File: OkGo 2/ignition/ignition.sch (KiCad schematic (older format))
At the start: 26 parts

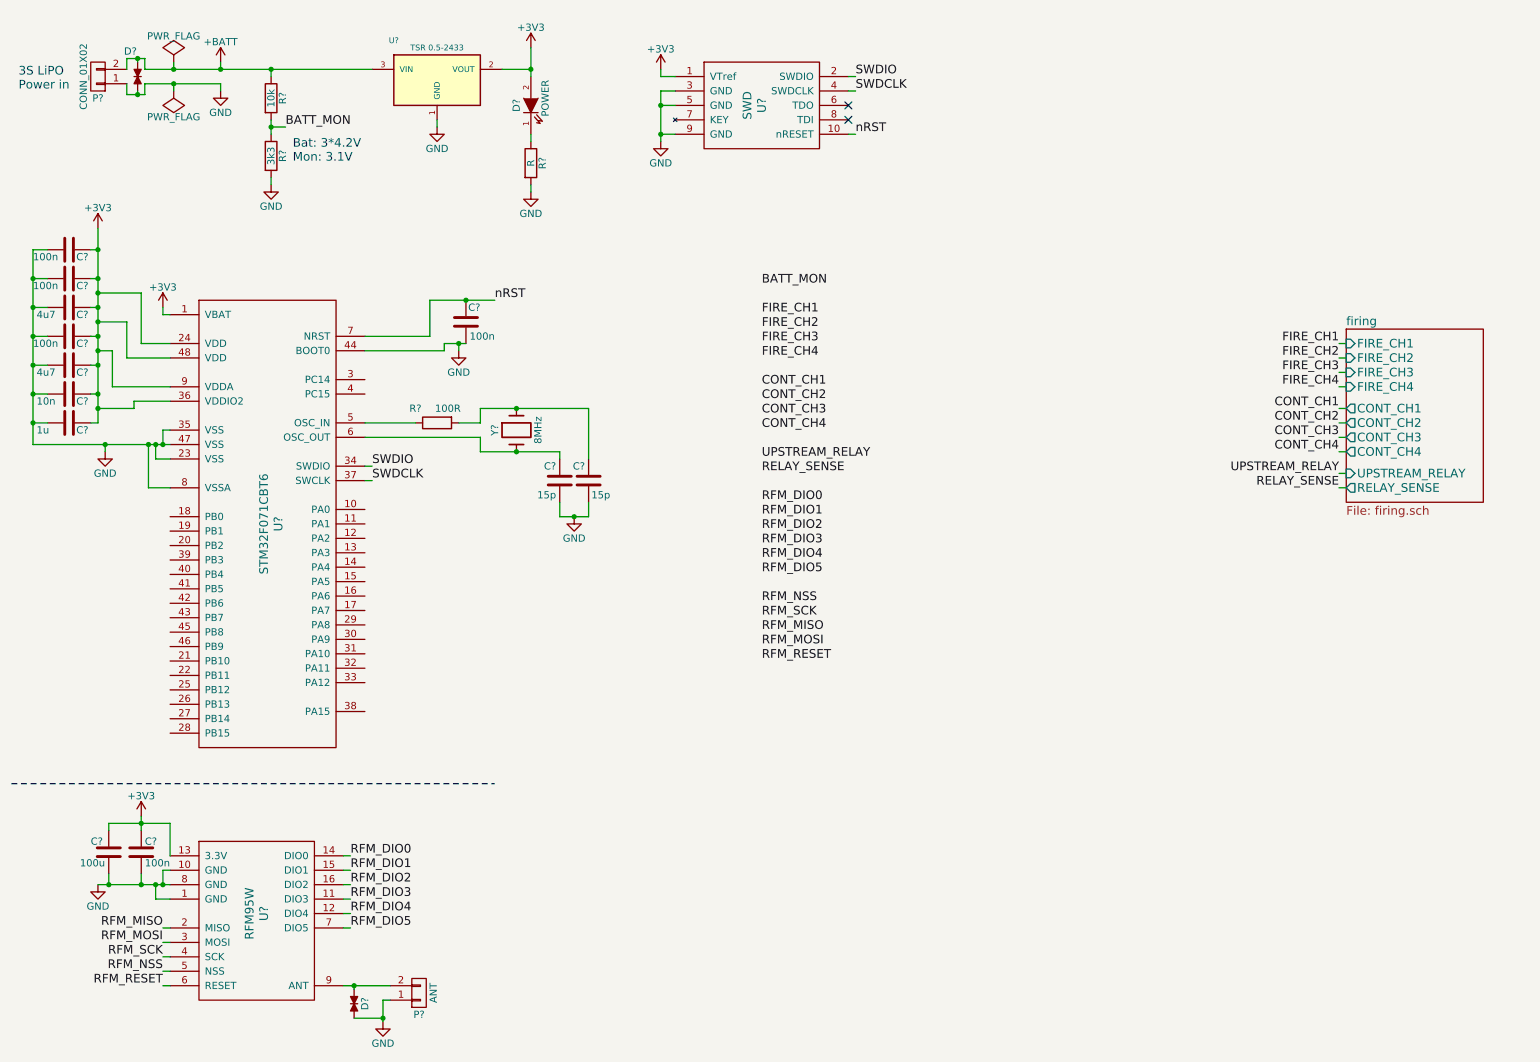
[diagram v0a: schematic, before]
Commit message: Removed pin labels from TVS
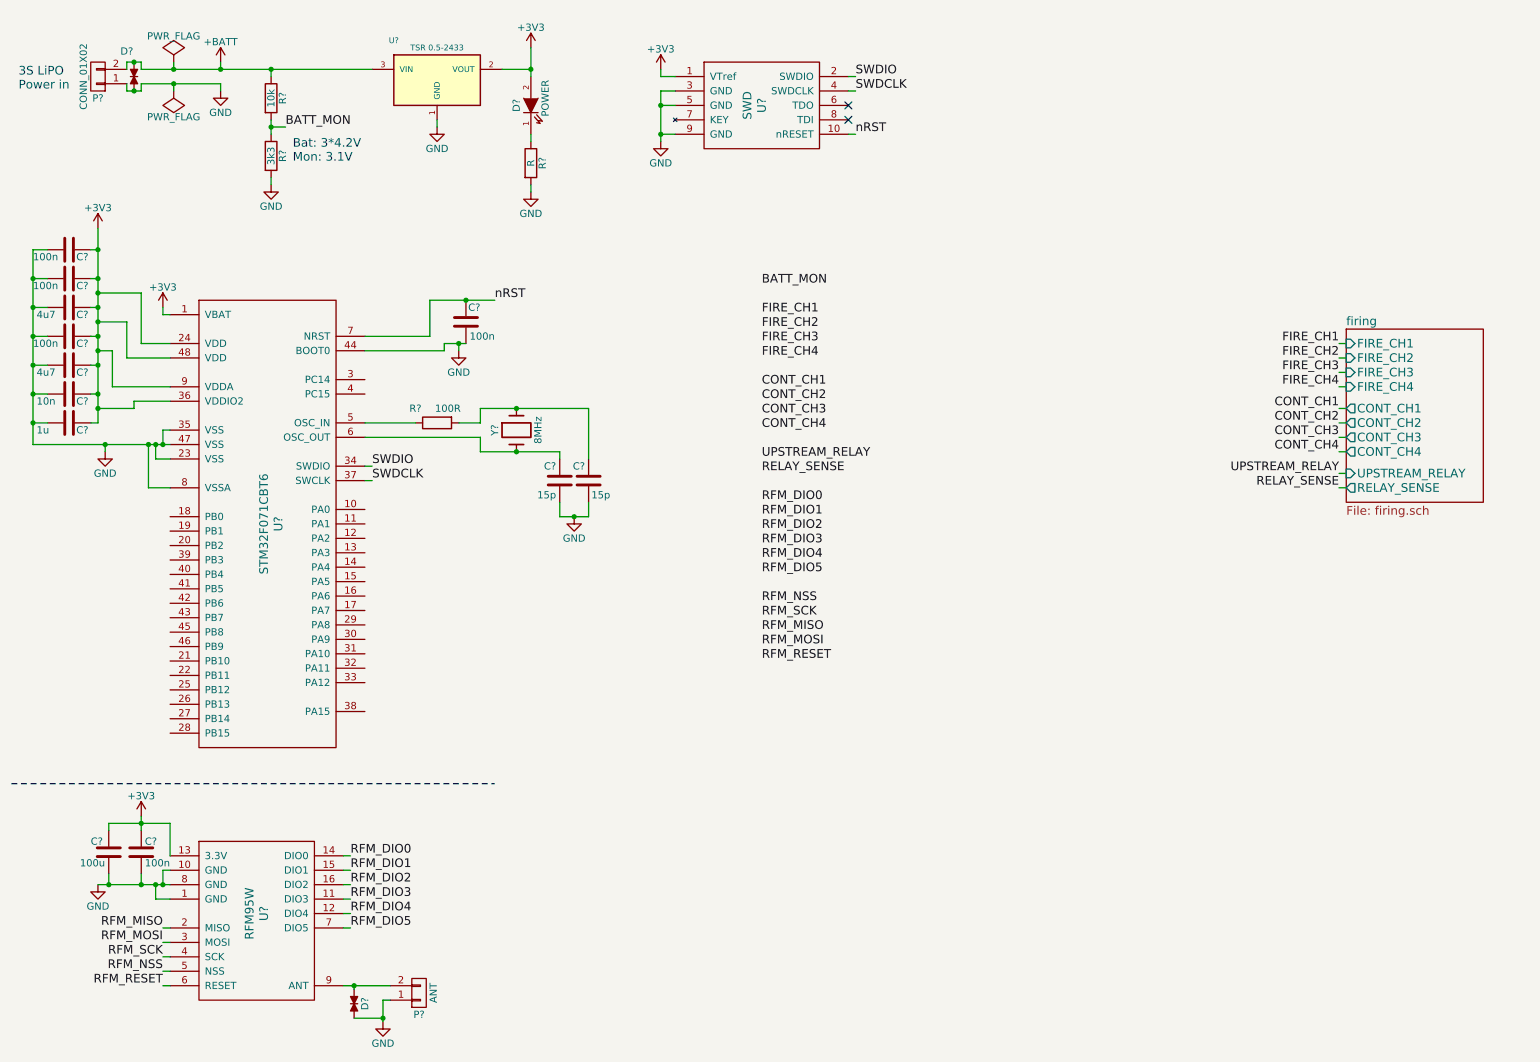
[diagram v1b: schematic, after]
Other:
- moved on the sheet: D?
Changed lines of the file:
@@
 L TVS_small D?
 U 1 1 559D6477
-P 1375 1000
-F 0 "D?" V 1200 950 50  0000 C CNN
-F 1 "TVS_small" H 1375 925 50  0001 C CNN
-F 2 "Resistors_SMD:R_0603_HandSoldering" H 1375 1000 60  0001 C CNN
-F 3 "" H 1375 1000 60  0000 C CNN
-F 4 "2368174" H 1375 1000 60  0001 C CNN "Farnell"
-	1    1375 1000
+P 1350 1000
+F 0 "D?" V 1175 950 50  0000 C CNN
+F 1 "TVS_small" H 1350 925 50  0001 C CNN
+F 2 "Resistors_SMD:R_0603_HandSoldering" H 1350 1000 60  0001 C CNN
+F 3 "" H 1350 1000 60  0000 C CNN
+F 4 "2368174" H 1350 1000 60  0001 C CNN "Farnell"
+	1    1350 1000
 	0    1    1    0
 $EndComp
@@
 	1625 1100 1625 1050
 Wire Wire Line
-	1425 1050 1950 1050
+	1400 1050 1625 1050
+Wire Wire Line
+	1625 1050 1950 1050
 Wire Wire Line
 	1950 950  1950 900
@@
 Connection ~ 1950 950
 Wire Wire Line
-	2300 1300 2300 1400
+	2300 1300 2300 1350
+Wire Wire Line
+	2300 1350 2300 1400
 Wire Wire Line
 	2300 1750 2300 1700
@@
 	3450 1350 3450 1300
 Wire Wire Line
-	4100 800  4100 1000
+	4100 800  4100 950
+Wire Wire Line
+	4100 950  4100 1000
 Wire Wire Line
 	4100 1400 4100 1450
@@
 	5000 1400 5100 1400
 Wire Wire Line
-	5000 1100 5000 1450
+	5000 1100 5000 1200
+Wire Wire Line
+	5000 1200 5000 1400
+Wire Wire Line
+	5000 1400 5000 1450
 Wire Wire Line
 	5100 1200 5000 1200
@@
 	6350 1400 6300 1400
 Wire Wire Line
-	1100 6600 1600 6600
+	1100 6600 1175 6600
+Wire Wire Line
+	1175 6600 1400 6600
+Wire Wire Line
+	1400 6600 1500 6600
+Wire Wire Line
+	1500 6600 1550 6600
+Wire Wire Line
+	1550 6600 1600 6600
 Wire Wire Line
 	1500 6600 1500 6700
@@
 Connection ~ 1550 6600
 Wire Wire Line
-	1400 6125 1400 6225
-Wire Wire Line
-	1175 6175 1600 6175
+	1400 6125 1400 6175
+Wire Wire Line
+	1400 6175 1400 6225
+Wire Wire Line
+	1175 6175 1400 6175
+Wire Wire Line
+	1400 6175 1600 6175
 Wire Wire Line
 	1600 6175 1600 6400
@@
 	3125 7400 3075 7400
 Wire Wire Line
-	3075 7400 3075 7550
-Wire Wire Line
-	2800 7300 3125 7300
+	3075 7400 3075 7525
+Wire Wire Line
+	3075 7525 3075 7550
+Wire Wire Line
+	2800 7300 2875 7300
+Wire Wire Line
+	2875 7300 3125 7300
 Wire Wire Line
 	1100 3200 1050 3200
 Wire Wire Line
-	1100 2050 1100 3400
+	1100 2050 1100 2200
+Wire Wire Line
+	1100 2200 1100 2400
+Wire Wire Line
+	1100 2400 1100 2500
+Wire Wire Line
+	1100 2500 1100 2600
+Wire Wire Line
+	1100 2600 1100 2700
+Wire Wire Line
+	1100 2700 1100 2800
+Wire Wire Line
+	1100 2800 1100 2900
+Wire Wire Line
+	1100 2900 1100 3000
+Wire Wire Line
+	1100 3000 1100 3200
+Wire Wire Line
+	1100 3200 1100 3300
+Wire Wire Line
+	1100 3300 1100 3400
 Connection ~ 1100 2400
 Connection ~ 1100 2600
@@
 	650  3200 750  3200
 Wire Wire Line
-	650  2200 650  3550
+	650  2200 650  2400
+Wire Wire Line
+	650  2400 650  2600
+Wire Wire Line
+	650  2600 650  2800
+Wire Wire Line
+	650  2800 650  3000
+Wire Wire Line
+	650  3000 650  3200
+Wire Wire Line
+	650  3200 650  3400
+Wire Wire Line
+	650  3400 650  3550
 Wire Wire Line
 	650  3000 750  3000
@@
 Connection ~ 650  2600
 Wire Wire Line
-	650  3550 1600 3550
+	650  3550 1150 3550
+Wire Wire Line
+	1150 3550 1450 3550
+Wire Wire Line
+	1450 3550 1500 3550
+Wire Wire Line
+	1500 3550 1550 3550
+Wire Wire Line
+	1550 3550 1600 3550
 Wire Wire Line
 	1550 3550 1550 3450
@@
 Connection ~ 1450 3550
 Wire Wire Line
-	3500 2850 3650 2850
+	3500 2850 3600 2850
+Wire Wire Line
+	3600 2850 3650 2850
 Wire Wire Line
 	3600 2850 3600 2900
 Connection ~ 3600 2850
 Wire Wire Line
-	3400 2550 3850 2550
+	3400 2550 3650 2550
+Wire Wire Line
+	3650 2550 3850 2550
 Wire Wire Line
 	3400 2550 3400 2800
@@
 	3750 3400 3750 3300
 Wire Wire Line
-	3750 3300 4500 3300
-Wire Wire Line
-	3750 3600 4300 3600
+	3750 3300 4000 3300
+Wire Wire Line
+	4000 3300 4500 3300
+Wire Wire Line
+	3750 3600 4000 3600
+Wire Wire Line
+	4000 3600 4300 3600
 Wire Wire Line
 	3750 3600 3750 3500
@@
 	4500 4050 4500 3950
 Wire Wire Line
-	4300 4050 4500 4050
+	4300 4050 4400 4050
+Wire Wire Line
+	4400 4050 4500 4050
 Wire Wire Line
 	4300 4050 4300 3950
@@
 	1175 6225 1175 6175
 Wire Wire Line
-	1425 950  3000 950
-Wire Wire Line
-	1300 875  1300 950
-Wire Wire Line
-	1300 1050 1300 1125
-Wire Wire Line
-	1425 1125 1425 1050
-Wire Wire Line
-	1425 875  1425 950
-Wire Wire Line
-	1300 875  1425 875
-Wire Wire Line
-	1375 875  1375 900
-Connection ~ 1375 875
-Wire Wire Line
-	1300 1125 1425 1125
-Wire Wire Line
-	1375 1125 1375 1100
-Connection ~ 1375 1125
+	1400 950  1625 950
+Wire Wire Line
+	1625 950  1950 950
+Wire Wire Line
+	1950 950  2300 950
+Wire Wire Line
+	2300 950  3000 950
+Wire Wire Line
+	1300 900  1300 950
+Wire Wire Line
+	1300 1050 1300 1100
+Wire Wire Line
+	1400 1100 1400 1050
+Wire Wire Line
+	1400 900  1400 950
+Wire Wire Line
+	1300 900  1350 900
+Wire Wire Line
+	1350 900  1400 900
+Wire Wire Line
+	1350 900  1350 900
+Connection ~ 1350 900
+Wire Wire Line
+	1300 1100 1350 1100
+Wire Wire Line
+	1350 1100 1400 1100
+Wire Wire Line
+	1350 1100 1350 1100
+Connection ~ 1350 1100
 Wire Wire Line
 	2875 7300 2875 7325

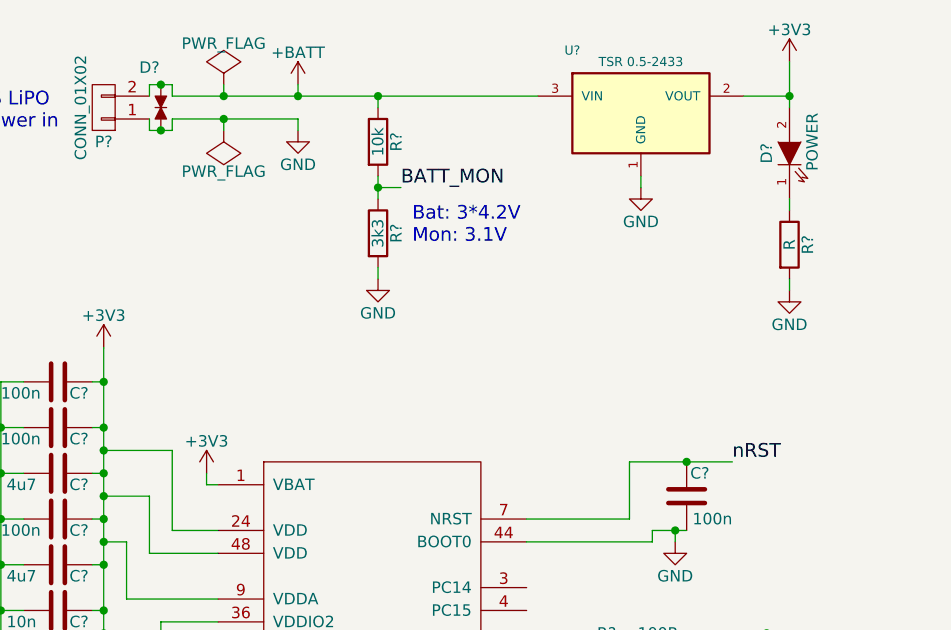
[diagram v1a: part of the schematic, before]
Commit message: Test points. Resolves #14
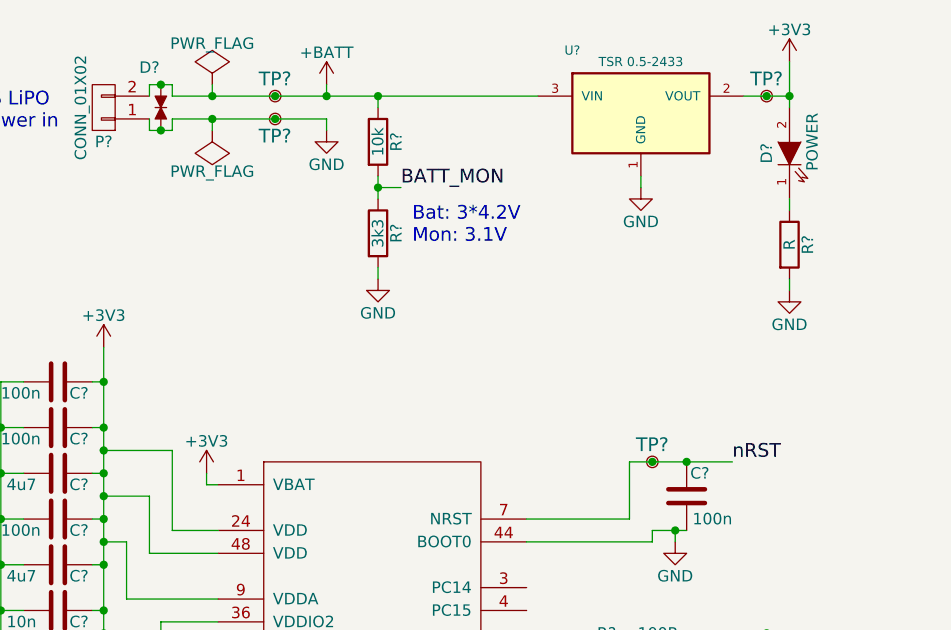
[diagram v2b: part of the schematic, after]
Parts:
- added TP? (x4): TestPoint, symbol TestPoint
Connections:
- net +3V3: now also TP?.1
- net +BATT: now also TP?.1
- net GND: now also TP?.1
- net nRST: now also TP?.1
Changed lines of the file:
@@
 LIBS:stm32f071cbt6
 LIBS:tvs_small
+LIBS:testpoint
 LIBS:ignition-cache
 EELAYER 25 0
@@
 L PWR_FLAG #FLG?
 U 1 1 5562BA6E
-P 1625 900
-F 0 "#FLG?" H 1625 995 50  0001 C CNN
-F 1 "PWR_FLAG" H 1625 1080 50  0000 C CNN
-F 2 "" H 1625 900 60  0000 C CNN
-F 3 "" H 1625 900 60  0000 C CNN
-	1    1625 900
+P 1575 900
+F 0 "#FLG?" H 1575 995 50  0001 C CNN
+F 1 "PWR_FLAG" H 1575 1080 50  0000 C CNN
+F 2 "" H 1575 900 60  0000 C CNN
+F 3 "" H 1575 900 60  0000 C CNN
+	1    1575 900
 	1    0    0    -1
 $EndComp
@@
 L PWR_FLAG #FLG?
 U 1 1 5562BA86
-P 1625 1100
-F 0 "#FLG?" H 1625 1195 50  0001 C CNN
-F 1 "PWR_FLAG" H 1625 1280 50  0000 C CNN
-F 2 "" H 1625 1100 60  0000 C CNN
-F 3 "" H 1625 1100 60  0000 C CNN
-	1    1625 1100
+P 1575 1100
+F 0 "#FLG?" H 1575 1195 50  0001 C CNN
+F 1 "PWR_FLAG" H 1575 1280 50  0000 C CNN
+F 2 "" H 1575 1100 60  0000 C CNN
+F 3 "" H 1575 1100 60  0000 C CNN
+	1    1575 1100
 	-1   0    0    1
 $EndComp
@@
 L +BATT #PWR?
 U 1 1 5562BAA1
-P 1950 900
-F 0 "#PWR?" H 1950 750 50  0001 C CNN
-F 1 "+BATT" H 1950 1040 50  0000 C CNN
-F 2 "" H 1950 900 60  0000 C CNN
-F 3 "" H 1950 900 60  0000 C CNN
-	1    1950 900
+P 2075 900
+F 0 "#PWR?" H 2075 750 50  0001 C CNN
+F 1 "+BATT" H 2075 1040 50  0000 C CNN
+F 2 "" H 2075 900 60  0000 C CNN
+F 3 "" H 2075 900 60  0000 C CNN
+	1    2075 900
 	1    0    0    -1
 $EndComp
@@
 L GND #PWR?
 U 1 1 5562BABE
-P 1950 1100
-F 0 "#PWR?" H 1950 850 50  0001 C CNN
-F 1 "GND" H 1950 950 50  0000 C CNN
-F 2 "" H 1950 1100 60  0000 C CNN
-F 3 "" H 1950 1100 60  0000 C CNN
-	1    1950 1100
+P 2075 1100
+F 0 "#PWR?" H 2075 850 50  0001 C CNN
+F 1 "GND" H 2075 950 50  0000 C CNN
+F 2 "" H 2075 1100 60  0000 C CNN
+F 3 "" H 2075 1100 60  0000 C CNN
+	1    2075 1100
 	1    0    0    -1
 $EndComp
@@
 $EndComp
 Wire Wire Line
-	1625 950  1625 900
-Wire Wire Line
-	1625 1100 1625 1050
-Wire Wire Line
-	1400 1050 1625 1050
-Wire Wire Line
-	1625 1050 1950 1050
-Wire Wire Line
-	1950 950  1950 900
-Connection ~ 1625 950
-Wire Wire Line
-	1950 1050 1950 1100
-Connection ~ 1625 1050
-Connection ~ 1950 950
+	1575 950  1575 900
+Wire Wire Line
+	1575 1100 1575 1050
+Wire Wire Line
+	1400 1050 1575 1050
+Wire Wire Line
+	1575 1050 2075 1050
+Wire Wire Line
+	2075 950  2075 900
+Connection ~ 1575 950
+Wire Wire Line
+	2075 1050 2075 1100
+Connection ~ 1575 1050
+Connection ~ 2075 950
 Wire Wire Line
 	2300 1300 2300 1350
@@
 	1175 6225 1175 6175
 Wire Wire Line
-	1400 950  1625 950
-Wire Wire Line
-	1625 950  1950 950
-Wire Wire Line
-	1950 950  2300 950
+	1400 950  1575 950
+Wire Wire Line
+	1575 950  2075 950
+Wire Wire Line
+	2075 950  2300 950
 Wire Wire Line
 	2300 950  3000 950
@@
 nRST
 Connection ~ 3650 2550
+$Comp
+L TestPoint TP?
+U 1 1 559DC01E
+P 1850 950
+F 0 "TP?" H 1850 875 60  0000 C CNN
+F 1 "TestPoint" H 1825 775 60  0001 C CNN
+F 2 "" H 1850 950 60  0000 C CNN
+F 3 "" H 1850 950 60  0000 C CNN
+	1    1850 950
+	-1   0    0    1
+$EndComp
+Connection ~ 1850 950
+$Comp
+L TestPoint TP?
+U 1 1 559DC0E8
+P 1850 1050
+F 0 "TP?" H 1850 975 60  0000 C CNN
+F 1 "TestPoint" H 1825 875 60  0001 C CNN
+F 2 "" H 1850 1050 60  0000 C CNN
+F 3 "" H 1850 1050 60  0000 C CNN
+	1    1850 1050
+	1    0    0    -1
+$EndComp
+Connection ~ 1850 1050
+$Comp
+L TestPoint TP?
+U 1 1 559DC42B
+P 4000 950
+F 0 "TP?" H 4000 875 60  0000 C CNN
+F 1 "TestPoint" H 3975 775 60  0001 C CNN
+F 2 "" H 4000 950 60  0000 C CNN
+F 3 "" H 4000 950 60  0000 C CNN
+	1    4000 950
+	-1   0    0    1
+$EndComp
+Connection ~ 4000 950
+$Comp
+L TestPoint TP?
+U 1 1 559DC7C1
+P 3500 2550
+F 0 "TP?" H 3500 2475 60  0000 C CNN
+F 1 "TestPoint" H 3475 2375 60  0001 C CNN
+F 2 "" H 3500 2550 60  0000 C CNN
+F 3 "" H 3500 2550 60  0000 C CNN
+	1    3500 2550
+	-1   0    0    1
+$EndComp
+Connection ~ 3500 2550
 $EndSCHEMATC
